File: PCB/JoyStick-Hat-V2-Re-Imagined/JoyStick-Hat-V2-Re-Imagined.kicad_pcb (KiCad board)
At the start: 4 copper layers, 123 x 56 mm, 113 parts, among them J1 20021121-00010C4LF, J10 0901301210, J11 0705430002, J12 DX07S016JA1R1500, J2 BU2032SM-JJ-GTR, J3 0901301210, J4 0901301108, J5 RJSAE-538A-02, J6 1757242, J7 SBH11-PBPC-D10-ST-BK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

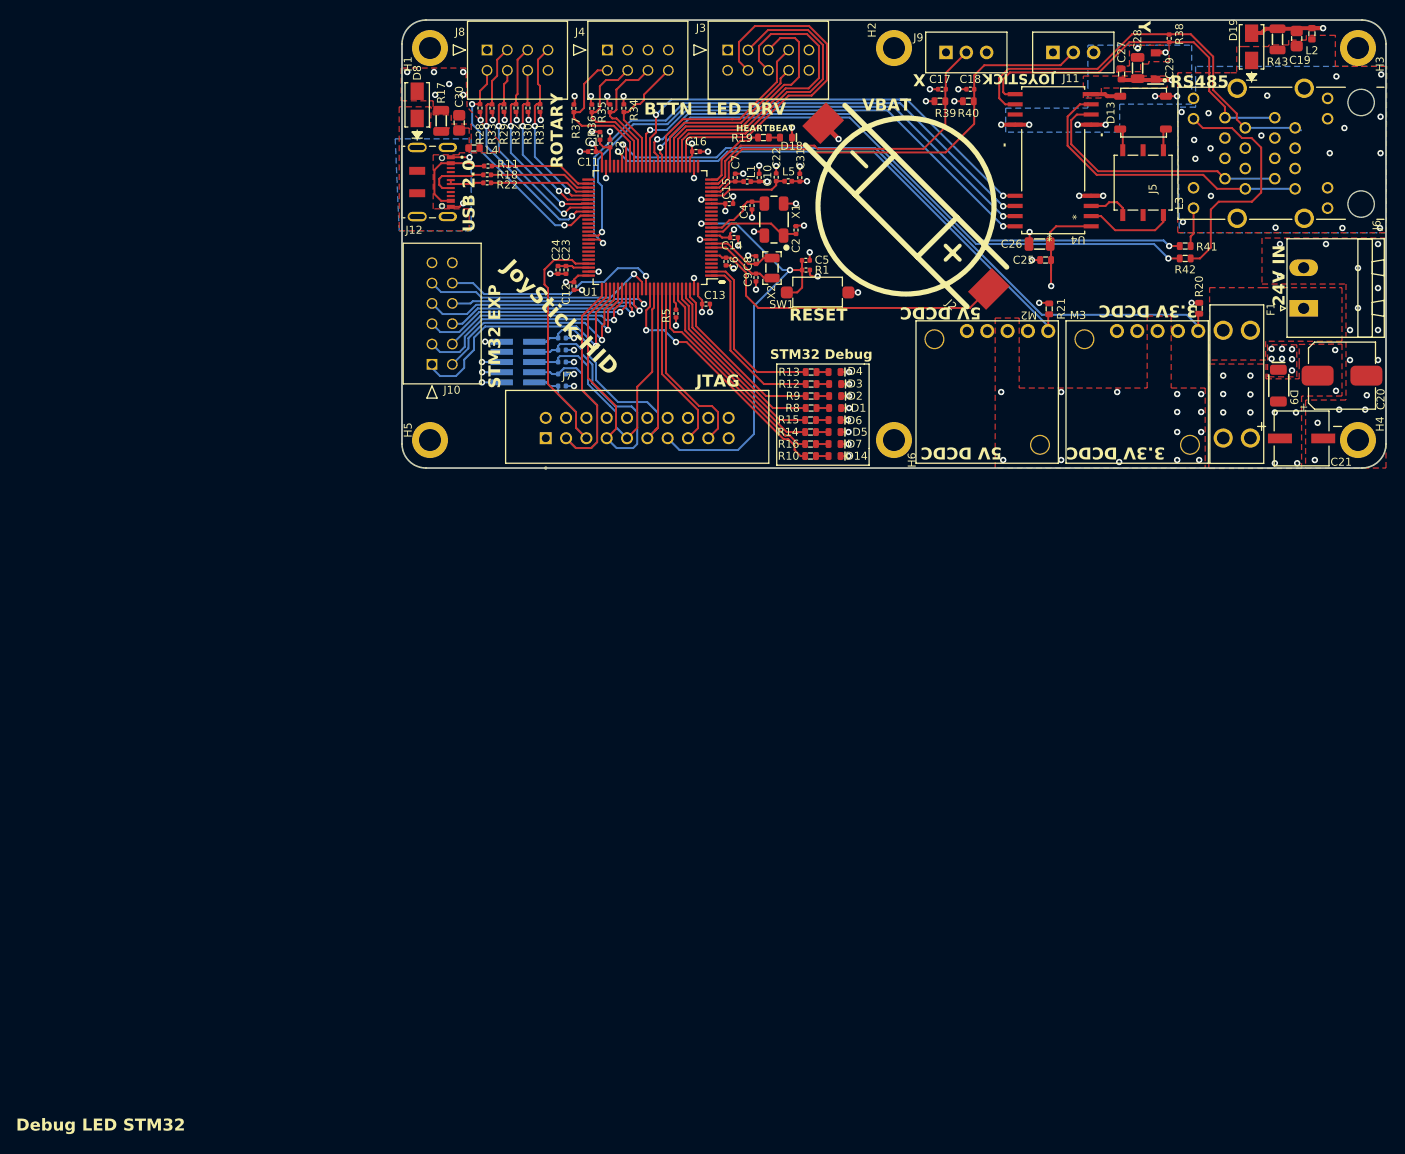
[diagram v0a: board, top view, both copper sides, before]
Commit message: Fab Fixes
Fixing for Frabrication, DRC cleared by pending external review subject to change.
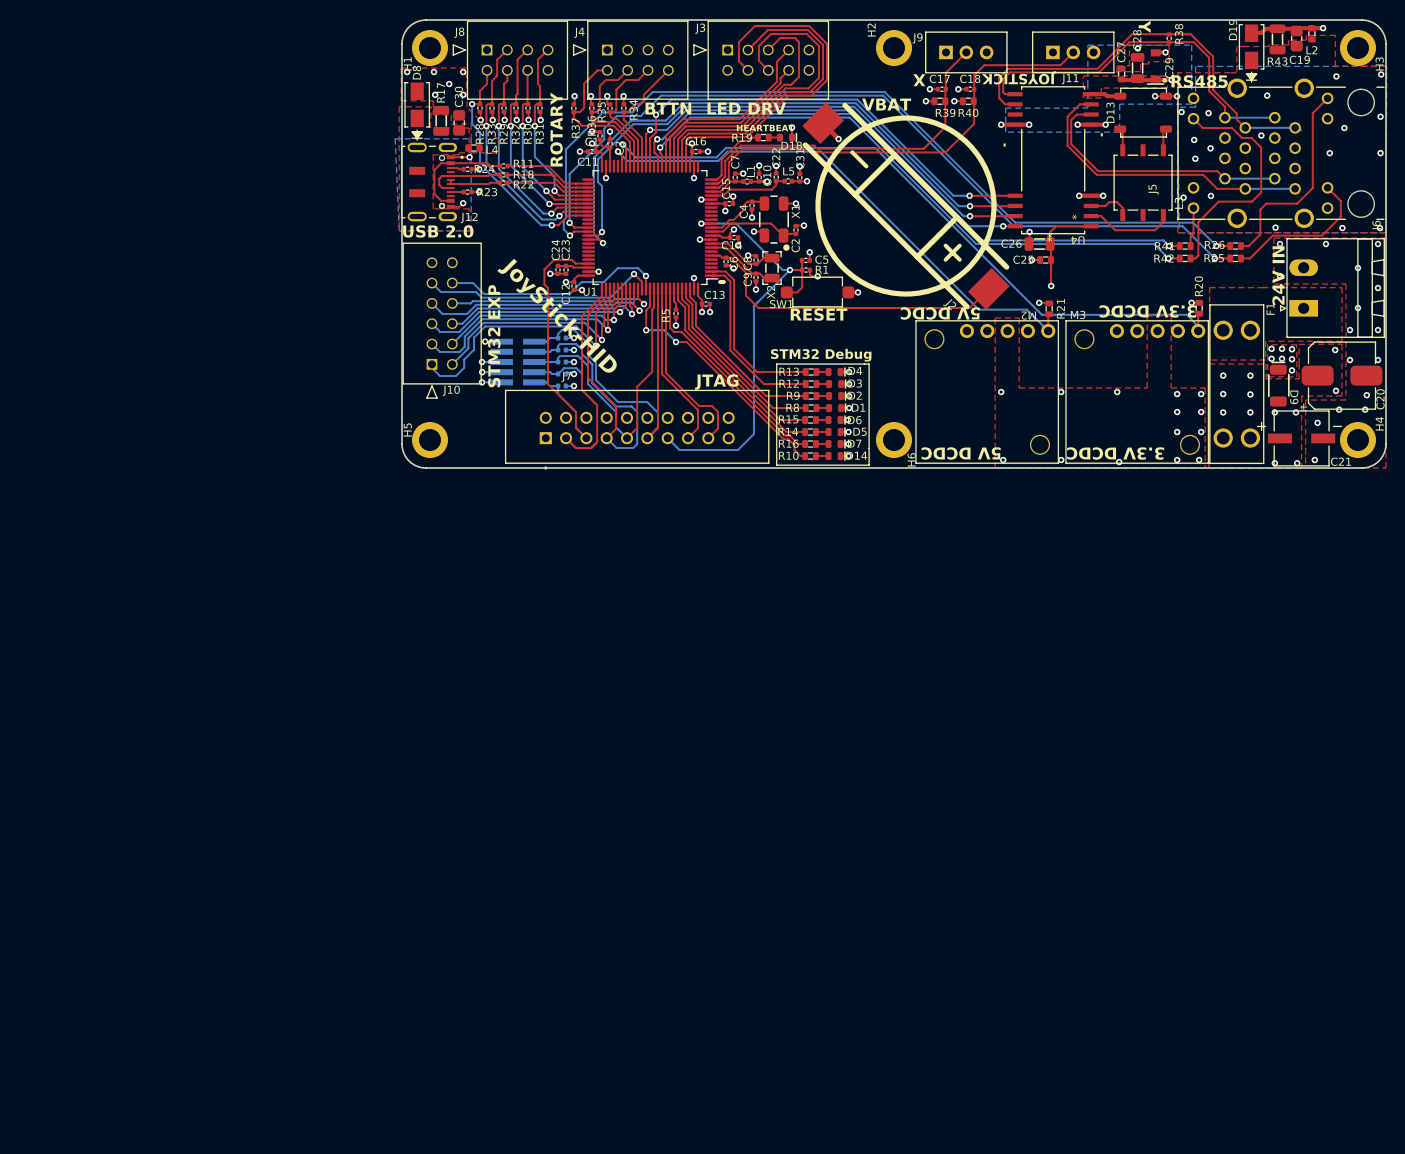
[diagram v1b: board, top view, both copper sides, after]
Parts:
- added R23: RC0402FR-075K1L, AVR-KiCAD-Lib-Resistors:R0402, F.Cu at (108.2, 75.5)
- added R24: RC0402FR-075K1L, AVR-KiCAD-Lib-Resistors:R0402, F.Cu at (108.2, 72.7)
- added R25: RC0603FR-07470RL, AVR-KiCAD-Lib-Resistors:R0603, F.Cu at (204.2, 83.8)
- added R26: RC0603FR-07470RL, AVR-KiCAD-Lib-Resistors:R0603, F.Cu at (204.2, 82.2)
- J10: value 0901301210 -> 0901301212
- moved R18 2.05 mm to (112.7, 73.3)
- moved R22 2.05 mm to (112.7, 74.3)
- moved R11 1.95 mm to (112.7, 72.2)
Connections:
- J12 pad 3: unconnected-(J12-CC1-Pad3) -> Net-(J12-CC1)
- J12 pad 9: unconnected-(J12-CC2-Pad9) -> Net-(J12-CC2)
- J5 pad 15: unconnected-(J5-Pad15) -> GND
- J5 pad 16: unconnected-(J5-Pad16) -> GND
- J5 pad 17: unconnected-(J5-Pad17) -> GND
- J5 pad 18: unconnected-(J5-Pad18) -> GND
- J5 pad 21: unconnected-(J5-Pad21) -> Net-(J5-Pad21)
- J5 pad 23: unconnected-(J5-Pad23) -> Net-(J5-Pad23)
- J5 pad 3: unconnected-(J5-Pad3) -> GND
- J5 pad 4: unconnected-(J5-Pad4) -> GND
- J5 pad 5: unconnected-(J5-Pad5) -> GND
- J5 pad 6: unconnected-(J5-Pad6) -> GND
- U1 pad 63: unconnected-(U1-PC6-Pad63) -> /RS485 To Motor Controller Interface/RS485_TX_LED2
- U1 pad 64: unconnected-(U1-PC7-Pad64) -> /RS485 To Motor Controller Interface/RS485_RX_LED2
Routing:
- net /RS485 To Motor Controller Interface/RS485_RX_LED2: track 0.00 -> 107.7 mm, vias 0 -> 2
- net /RS485 To Motor Controller Interface/RS485_TX_LED2: track 0.00 -> 104.6 mm, vias 0 -> 2
- net Net-(J5-Pad21): track 0.00 -> 25.8 mm
- net Net-(J5-Pad23): track 0.00 -> 18.9 mm
- net Net-(J12-D--Pad5): track 8.09 -> 10.1 mm
- net Net-(J12-D+-Pad6): track 4.63 -> 6.68 mm
- net Net-(U1-PB15): track 12.6 -> 10.6 mm
- net Net-(J12-VBUS-Pad11): track 12.1 -> 14.1 mm
- net Net-(U1-PB13): track 13.0 -> 11.1 mm
- net GND: track 75.0 -> 76.9 mm, vias 81 -> 83
- net Net-(U1-PB14): track 12.9 -> 10.9 mm
- net Net-(J12-CC1): track 0.00 -> 1.68 mm
- net Net-(J12-CC2): track 0.00 -> 1.62 mm
- net /JoyStick Interface/ROTARY2_POLE2: track 25.6 -> 27.2 mm
- net /JoyStick Interface/ROTARY1_POLE3: track 30.4 -> 31.7 mm
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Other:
- board text removed: "Debug LED STM32"

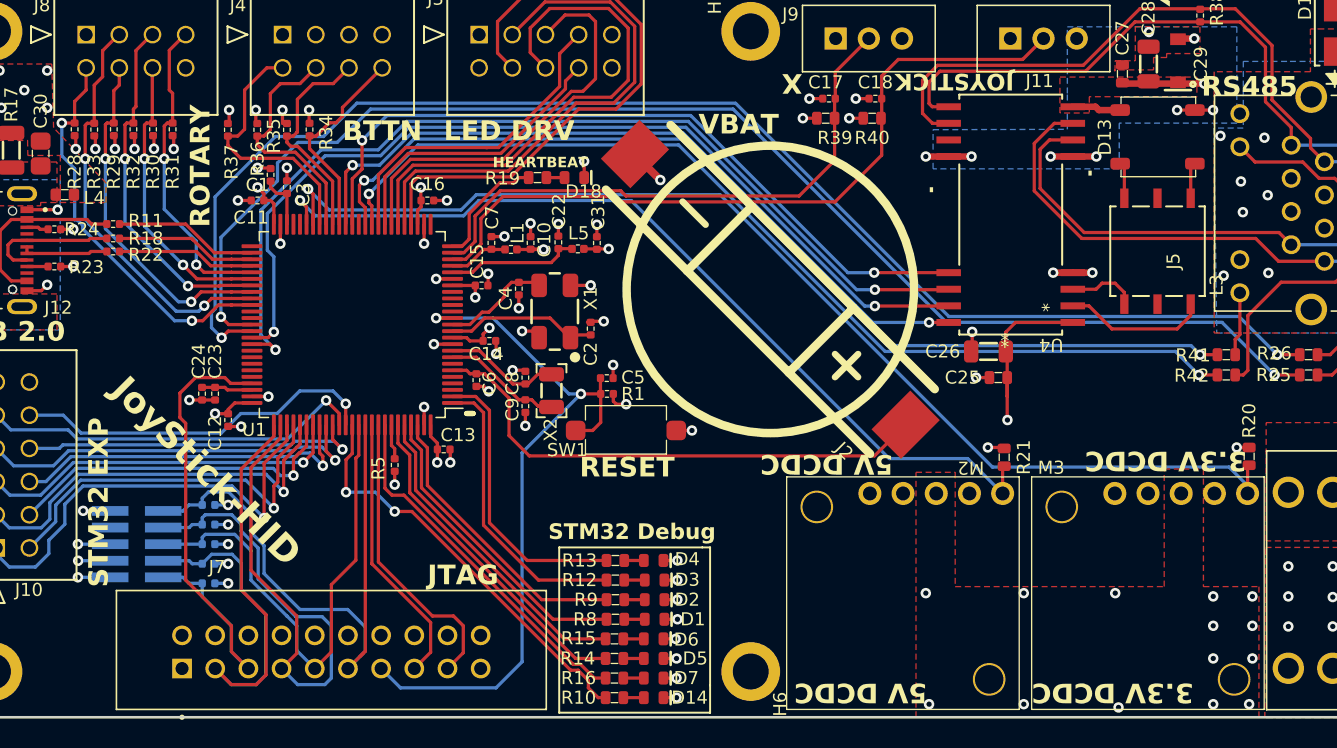
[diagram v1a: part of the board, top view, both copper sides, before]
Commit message: STM32 Exp
Removed 5V regulator, corrected RS485 schematic,  added more expansion to STM32 since we had space.
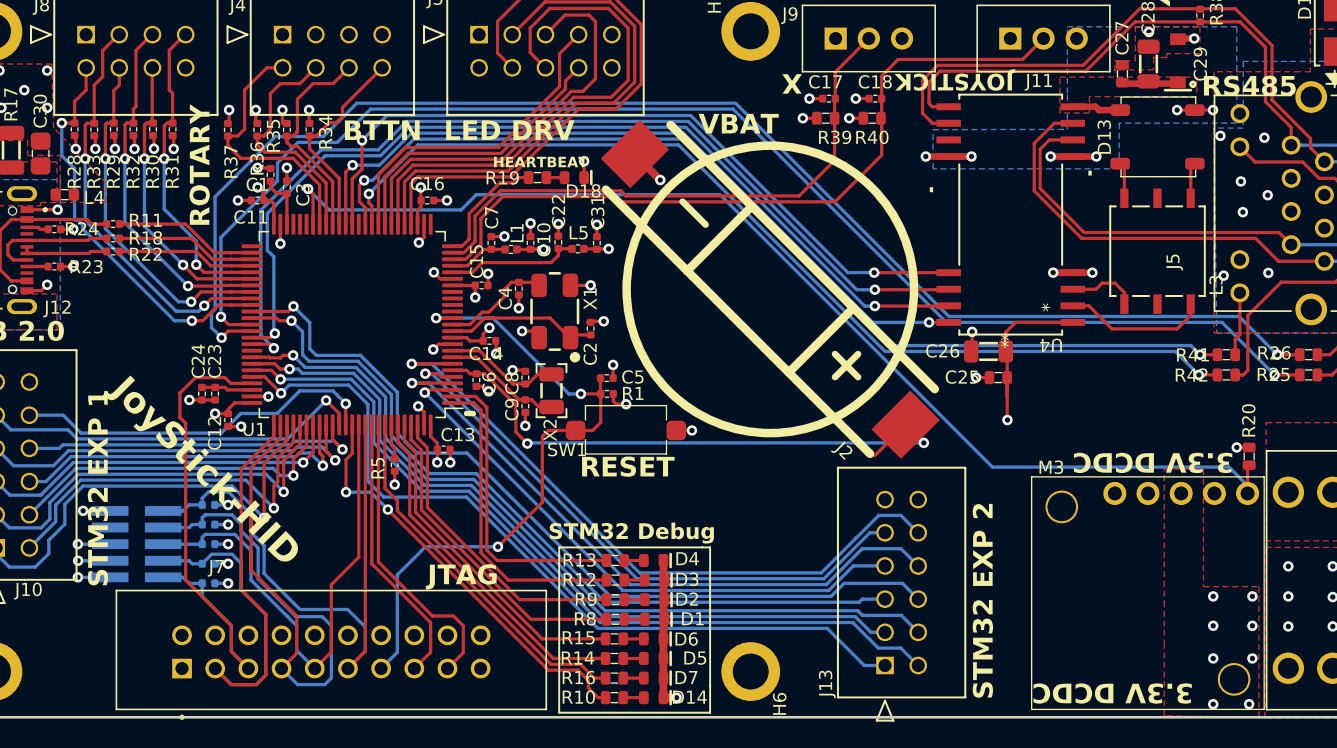
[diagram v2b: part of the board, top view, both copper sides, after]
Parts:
- removed M2: D24V22F5, AVR-KiCAD-Lib-Modules:D24V22F12
- removed R21: RC0603FR-072K2L, AVR-KiCAD-Lib-Resistors:R0603
- added J13: 0901301212, AVR-KiCAD-Lib-Connectors:CON_901301212_MOL, F.Cu at (171.8, 106.0)
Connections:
- U1 pad 3: unconnected-(U1-PE4-Pad3) -> /STM32F446RET6-MCU/PE4
- U1 pad 4: unconnected-(U1-PE5-Pad4) -> /STM32F446RET6-MCU/PE5
- U1 pad 45: /Power/5V_PG -> /STM32F446RET6-MCU/5V_PG
- U1 pad 5: unconnected-(U1-PE6-Pad5) -> /STM32F446RET6-MCU/PE6
- U1 pad 61: unconnected-(U1-PD14-Pad61) -> /STM32F446RET6-MCU/PD14
- U1 pad 62: unconnected-(U1-PD15-Pad62) -> /STM32F446RET6-MCU/PD15
- U1 pad 68: unconnected-(U1-PA9-Pad68) -> /STM32F446RET6-MCU/PA9
- U1 pad 69: unconnected-(U1-PA10-Pad69) -> /STM32F446RET6-MCU/PA10
- U1 pad 7: unconnected-(U1-PC13-Pad7) -> /STM32F446RET6-MCU/PC13
- U1 pad 70: unconnected-(U1-PA11-Pad70) -> /STM32F446RET6-MCU/PA11
- U1 pad 71: unconnected-(U1-PA12-Pad71) -> /STM32F446RET6-MCU/PA12
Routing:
- net /Power/5V_PG: track 68.0 -> 0.00 mm, vias 1 -> 0
- net /STM32F446RET6-MCU/PD14: track 0.00 -> 64.3 mm, vias 0 -> 1
- net /STM32F446RET6-MCU/PA11: track 0.00 -> 62.2 mm, vias 0 -> 1
- net /STM32F446RET6-MCU/PA9: track 0.00 -> 61.7 mm, vias 0 -> 1
- net /STM32F446RET6-MCU/PA12: track 0.00 -> 61.6 mm, vias 0 -> 1
- net /STM32F446RET6-MCU/PD15: track 0.00 -> 60.4 mm, vias 0 -> 1
- net /STM32F446RET6-MCU/PA10: track 0.00 -> 58.8 mm, vias 0 -> 1
- net +5V: track 59.9 -> 8.11 mm, vias 1 -> 0
- net /STM32F446RET6-MCU/PC13: track 0.00 -> 51.2 mm, vias 0 -> 1
- net /STM32F446RET6-MCU/PE5: track 0.00 -> 49.9 mm, vias 0 -> 1
- net /STM32F446RET6-MCU/PE6: track 0.00 -> 45.4 mm, vias 0 -> 1
- net /STM32F446RET6-MCU/PE4: track 0.00 -> 44.5 mm, vias 0 -> 1
- net /STM32F446RET6-MCU/NRST: track 56.4 -> 50.7 mm, vias 2 -> 3
- net /STM32F446RET6-MCU/VBAT: track 40.1 -> 45.0 mm, vias 0 -> 2
- net GND: track 76.9 -> 81.3 mm, vias 83 -> 76
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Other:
- board text added: "STM32 EXP 1"
- board text added: "STM32 EXP 2"
- board text removed: "5V DCDC"
- board text removed: "5V PG"
- board text removed: "5V Rail"
- board text removed: "STM32 EXP"

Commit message: RS485 Circuit Fixes, STM32 Expansion
Fixe RS485 circuit errors, changed PCB topology for RS485. Added STM32 expansion IO in place of 5V Regulator.
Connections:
- C19 pad 2: GND -> Earth
- D19 pad 2: GND -> Earth
- J5 pad 15: GND -> Earth
- J5 pad 16: GND -> Earth
- J5 pad 17: GND -> Earth
- J5 pad 18: GND -> Earth
- J5 pad 24: (no net) -> GND
- J5 pad 3: GND -> Earth
- J5 pad 4: GND -> Earth
- J5 pad 5: GND -> Earth
- J5 pad 6: GND -> Earth
- L2 pad 2: GND -> Earth
- R43 pad 1: GND -> Earth
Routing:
- net GND: track 81.3 -> 106.1 mm, vias 76 -> 74
- net Earth: track 11.0 -> 20.3 mm, vias 8 -> 32
- net Net-(J5-Pad21): track 25.8 -> 26.3 mm
- net /RS485 To Motor Controller Interface/RJ45_SHIELD: vias 17 -> 19
- added copper zone on In1.Cu, net Earth
- added copper zone on In2.Cu, net Earth
- added copper zone on In2.Cu, net GND
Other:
- board text added: "PA10"
- board text added: "PA11"
- board text added: "PA12"
- board text added: "PA9"
- board text added: "PC13"
- board text added: "PD14"
- board text added: "PD15"
- board text added: "PE4"
- board text added: "PE5"
- board text added: "PE6"
